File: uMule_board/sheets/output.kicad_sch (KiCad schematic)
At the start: 10 parts, among them J3 OUT3, Q3 AON6407, U24 EL3H7(B)(TA)-G

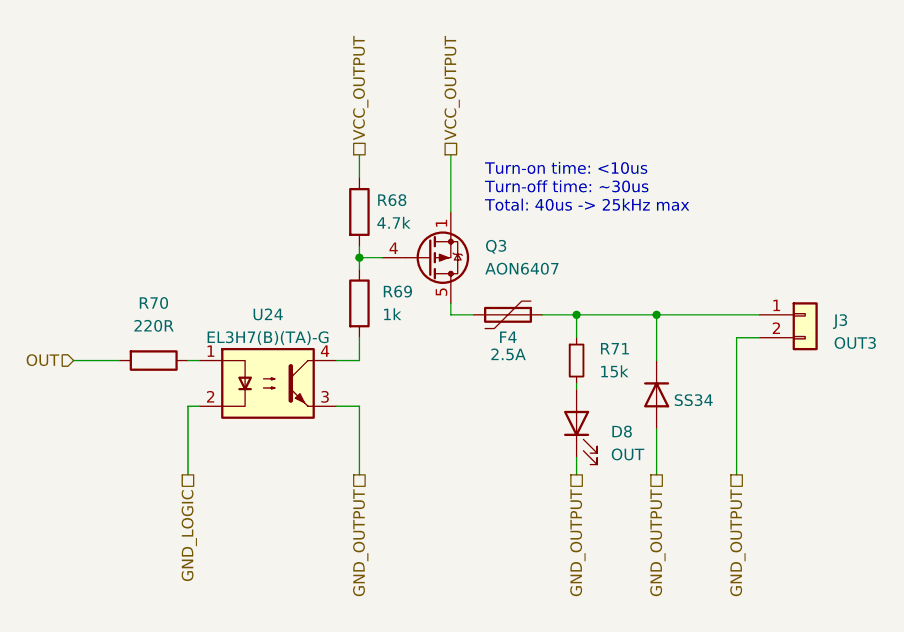
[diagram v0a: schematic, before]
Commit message: Started working on PCB. Ditched high power outputs. Focusing on photodiodes. One commit closer to order
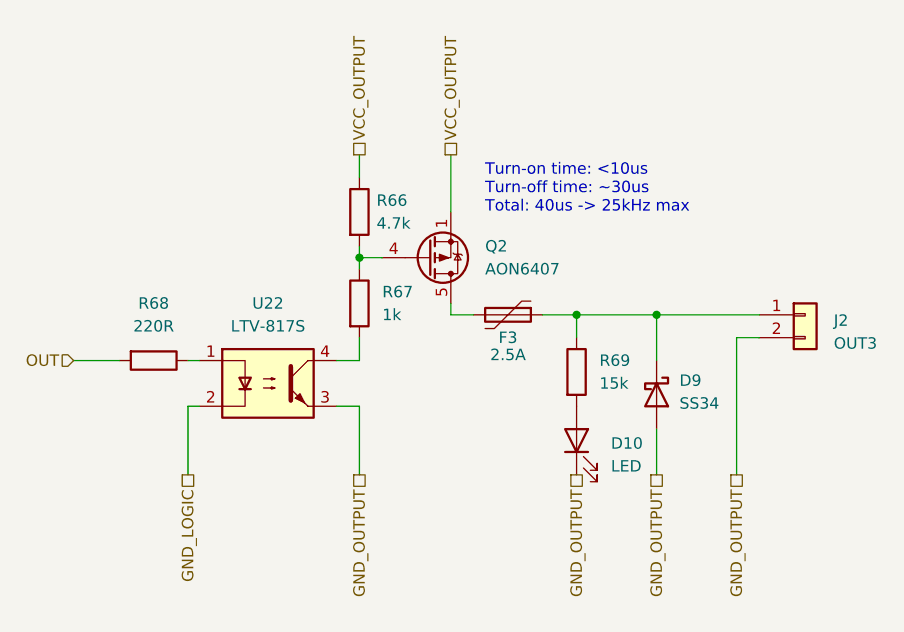
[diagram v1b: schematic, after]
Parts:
- removed D1: SS34, Diode_SMD:D_SMA, symbol Device:D
- removed D8: OUT, LED_SMD:LED_0603_1608Metric, symbol Device:LED
- removed R71: 15k, Resistor_SMD:R_0603_1608Metric, symbol Device:R_Small
- removed U24: EL3H7(B)(TA)-G, Package_SO:SOP-4_4.4x2.6mm_P1.27mm, symbol Isolator:PC817
- added D10: LED, LED_SMD:LED_0603_1608Metric_Pad1.05x0.95mm_HandSolder, symbol Device:LED
- added D9: SS34, Diode_SMD:D_SMA, symbol Diode:SS34
- added R69: 15k, Resistor_SMD:R_0603_1608Metric, symbol Device:R
- added U22: LTV-817S, Package_DIP:SMDIP-4_W9.53mm_Clearance8mm, symbol Isolator:LTV-817S
- renumbered F4 to F3, J3 to J2, Q3 to Q2, R68 to R66, R69 to R67, R70 to R68
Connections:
- net GND_LOGIC: now also U22.2
- net GND_OUTPUT: now also D10.1 (K), D9.2 (A), U22.3
- net at F3.1, J2.1 (Pin_1): now also D9.1 (K), R69.1
- net at R68.1: now also U22.1
- net at R67.2: now also U22.4
- new net: D10.2 (A), R69.2
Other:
- title: (none) -> uMule_board
